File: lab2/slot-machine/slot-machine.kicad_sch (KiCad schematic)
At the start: 22 parts

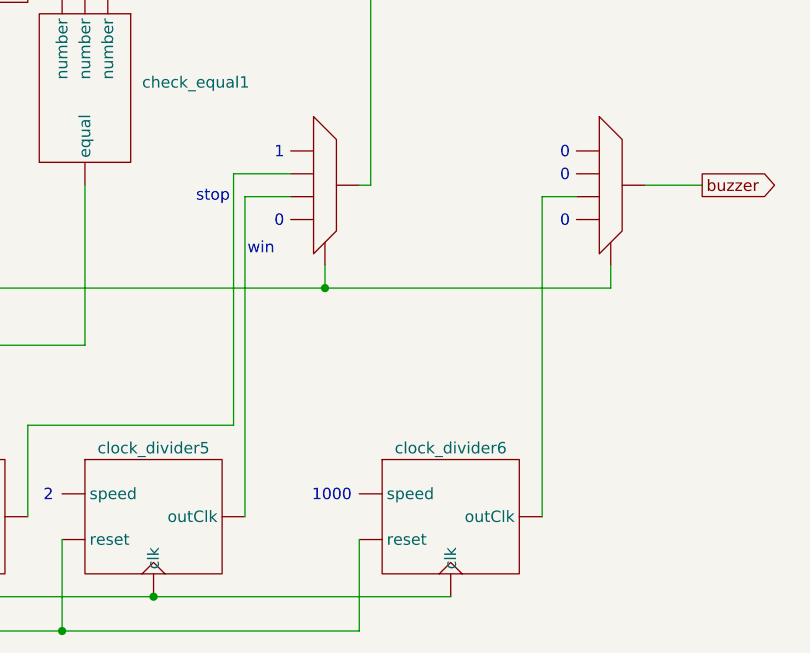
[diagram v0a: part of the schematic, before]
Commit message: update block diagram
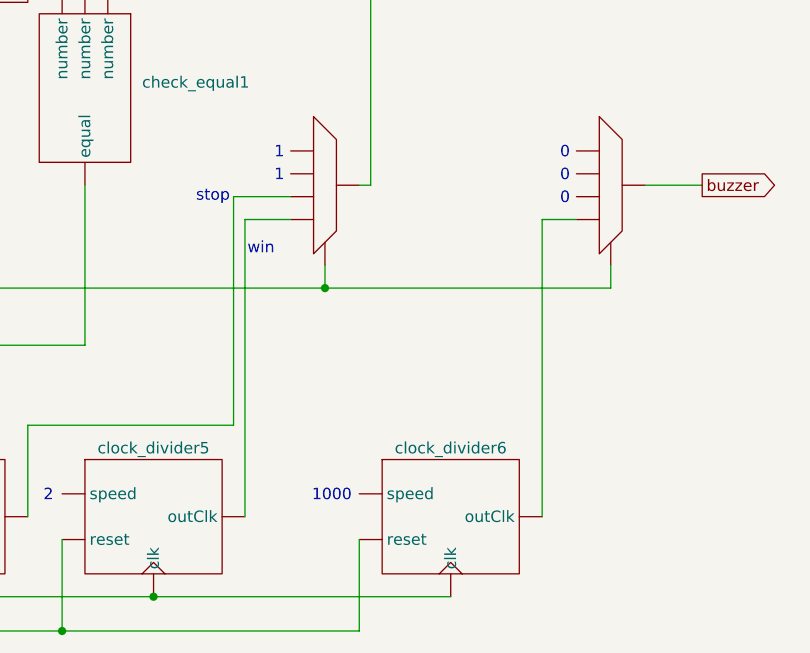
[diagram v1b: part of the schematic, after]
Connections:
- net at LFSR3. (reset): now also bin_to_bcd3. (bin), check_equal1. (number); no longer clock_divider3. (speed)
- net at U1.: now also FSM1. (start/stop), U2.
- net at bin_to_bcd2. (bin): now also 7_seg_encoder3. (en); no longer 7_seg_encoder4. (en)
- net at bin_to_bcd3. (bin): now also 7_seg_encoder5. (en); no longer 7_seg_encoder6. (en)
- net at bin_to_bcd1. (bin): now also 7_seg_encoder2. (en); no longer 7_seg_encoder1. (en)
- new net: FSM1. (start/stop), LFSR1. (reset), LFSR2. (reset), LFSR3. (reset), clock_divider1. (speed), clock_divider2. (speed), clock_divider3. (speed), clock_divider4. (speed), clock_divider5. (speed), clock_divider6. (speed)
- new net: FSM1. (start/stop), LFSR1. (reset), LFSR2. (reset), LFSR3. (reset)
- new net: LFSR1. (reset), bin_to_bcd1. (bin), check_equal1. (number)
- new net: LFSR3. (reset), clock_divider3. (speed)
- new net: LFSR2. (reset), bin_to_bcd2. (bin), check_equal1. (number)
- new net: 7_seg_encoder1. (en), 7_seg_encoder2. (en), 7_seg_encoder3. (en), 7_seg_encoder4. (en), 7_seg_encoder5. (en), 7_seg_encoder6. (en), U1.
- new net: U1., clock_divider5. (speed)
- new net: U1., clock_divider4. (speed)
- new net: 7_seg_encoder4. (en), bin_to_bcd2. (bin)
- new net: 7_seg_encoder6. (en), bin_to_bcd3. (bin)
- new net: 7_seg_encoder1. (en), bin_to_bcd1. (bin)
- new net: U2., clock_divider6. (speed)
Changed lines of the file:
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@@
 	(wire
 		(pts
-			(xy 133.35 140.97) (xy 133.35 105.41)
+			(xy 133.35 140.97) (xy 133.35 107.95)
 		)
 		(stroke
@@
 	(wire
 		(pts
-			(xy 133.35 105.41) (xy 137.16 105.41)
+			(xy 133.35 107.95) (xy 137.16 107.95)
 		)
 		(stroke
@@
 	(wire
 		(pts
-			(xy 100.33 105.41) (xy 105.41 105.41)
-		)
-		(stroke
-			(width 0)
-			(type default)
-		)
-	)
-	(wire
-		(pts
-			(xy 99.06 130.81) (xy 99.06 102.87)
+			(xy 100.33 107.95) (xy 105.41 107.95)
+		)
+		(stroke
+			(width 0)
+			(type default)
+		)
+	)
+	(wire
+		(pts
+			(xy 99.06 130.81) (xy 99.06 105.41)
 		)
 		(stroke
@@
 	(wire
 		(pts
-			(xy 100.33 140.97) (xy 100.33 105.41)
+			(xy 100.33 140.97) (xy 100.33 107.95)
 		)
 		(stroke
@@
 	(wire
 		(pts
-			(xy 99.06 102.87) (xy 105.41 102.87)
+			(xy 99.06 105.41) (xy 105.41 105.41)
 		)
 		(stroke
@@
 		)
 	)
+	(text "10"
+		(exclude_from_sim no)
+		(at 27.432 54.864 0)
+		(effects
+			(font
+				(size 1.27 1.27)
+			)
+		)
+	)
+	(text "stop"
+		(exclude_from_sim no)
+		(at 96.774 105.41 0)
+		(effects
+			(font
+				(size 1.27 1.27)
+			)
+		)
+	)
+	(text "7-bit"
+		(exclude_from_sim no)
+		(at 82.55 77.47 0)
+		(effects
+			(font
+				(size 1.27 1.27)
+			)
+		)
+	)
+	(text "7-bit"
+		(exclude_from_sim no)
+		(at 83.058 56.134 0)
+		(effects
+			(font
+				(size 1.27 1.27)
+			)
+		)
+	)
+	(text "1000"
+		(exclude_from_sim no)
+		(at 109.982 138.684 0)
+		(effects
+			(font
+				(size 1.27 1.27)
+			)
+		)
+	)
+	(text "5"
+		(exclude_from_sim no)
+		(at 28.194 33.274 0)
+		(effects
+			(font
+				(size 1.27 1.27)
+			)
+		)
+	)
 	(text "0"
 		(exclude_from_sim no)
-		(at 135.89 108.204 0)
-		(effects
-			(font
-				(size 1.27 1.27)
-			)
-		)
-	)
-	(text "10"
-		(exclude_from_sim no)
-		(at 27.432 54.864 0)
+		(at 135.89 100.584 0)
+		(effects
+			(font
+				(size 1.27 1.27)
+			)
+		)
+	)
+	(text "7-bit"
+		(exclude_from_sim no)
+		(at 83.058 34.544 0)
+		(effects
+			(font
+				(size 1.27 1.27)
+			)
+		)
+	)
+	(text "1"
+		(exclude_from_sim no)
+		(at 54.356 138.684 0)
+		(effects
+			(font
+				(size 1.27 1.27)
+			)
+		)
+	)
+	(text "2-bit"
+		(exclude_from_sim no)
+		(at 61.214 114.3 0)
+		(effects
+			(font
+				(size 1.27 1.27)
+			)
+		)
+	)
+	(text "20"
+		(exclude_from_sim no)
+		(at 27.432 76.454 0)
+		(effects
+			(font
+				(size 1.27 1.27)
+			)
+		)
+	)
+	(text "1"
+		(exclude_from_sim no)
+		(at 104.14 103.124 0)
 		(effects
 			(font
@@
 	(text "0"
 		(exclude_from_sim no)
-		(at 104.14 108.204 0)
-		(effects
-			(font
-				(size 1.27 1.27)
-			)
-		)
-	)
-	(text "stop"
-		(exclude_from_sim no)
-		(at 96.774 105.41 0)
-		(effects
-			(font
-				(size 1.27 1.27)
-			)
-		)
-	)
-	(text "7-bit"
-		(exclude_from_sim no)
-		(at 82.55 77.47 0)
-		(effects
-			(font
-				(size 1.27 1.27)
-			)
-		)
-	)
-	(text "7-bit"
-		(exclude_from_sim no)
-		(at 83.058 56.134 0)
-		(effects
-			(font
-				(size 1.27 1.27)
-			)
-		)
-	)
-	(text "1000"
-		(exclude_from_sim no)
-		(at 109.982 138.684 0)
-		(effects
-			(font
-				(size 1.27 1.27)
-			)
-		)
-	)
-	(text "5"
-		(exclude_from_sim no)
-		(at 28.194 33.274 0)
-		(effects
-			(font
-				(size 1.27 1.27)
-			)
-		)
-	)
-	(text "0"
-		(exclude_from_sim no)
-		(at 135.89 100.584 0)
-		(effects
-			(font
-				(size 1.27 1.27)
-			)
-		)
-	)
-	(text "7-bit"
-		(exclude_from_sim no)
-		(at 83.058 34.544 0)
-		(effects
-			(font
-				(size 1.27 1.27)
-			)
-		)
-	)
-	(text "1"
-		(exclude_from_sim no)
-		(at 54.356 138.684 0)
-		(effects
-			(font
-				(size 1.27 1.27)
-			)
-		)
-	)
-	(text "2-bit"
-		(exclude_from_sim no)
-		(at 61.214 114.3 0)
-		(effects
-			(font
-				(size 1.27 1.27)
-			)
-		)
-	)
-	(text "20"
-		(exclude_from_sim no)
-		(at 27.432 76.454 0)
+		(at 135.89 105.664 0)
 		(effects
 			(font
@@
 	)
 	(symbol
-		(lib_name "slot-machine:seven_seg_encoder")
 		(lib_id "slot-machine:seven_seg_encoder")
 		(at 125.73 60.96 0)
@@
 	)
 	(symbol
-		(lib_name "slot-machine:seven_seg_encoder")
 		(lib_id "slot-machine:seven_seg_encoder")
 		(at 125.73 78.74 0)
@@
 	)
 	(symbol
-		(lib_name "slot-machine:clock_divider")
 		(lib_id "slot-machine:clock_divider")
 		(at 90.17 140.97 0)
@@
 	)
 	(symbol
-		(lib_name "slot-machine:seven_seg_encoder")
 		(lib_id "slot-machine:seven_seg_encoder")
 		(at 125.73 34.29 0)
@@
 	)
 	(symbol
-		(lib_name "slot-machine:clock_divider")
 		(lib_id "slot-machine:clock_divider")
 		(at 66.04 140.97 0)
@@
 	)
 	(symbol
-		(lib_name "slot-machine:clock_divider")
 		(lib_id "slot-machine:clock_divider")
 		(at 123.19 140.97 0)
@@
 	)
 	(symbol
-		(lib_name "slot-machine:seven_seg_encoder")
 		(lib_id "slot-machine:seven_seg_encoder")
 		(at 125.73 69.85 0)
@@
 	)
 	(symbol
-		(lib_name "slot-machine:seven_seg_encoder")
 		(lib_id "slot-machine:seven_seg_encoder")
 		(at 125.73 43.18 0)
@@
 	)
 	(symbol
-		(lib_name "slot-machine:seven_seg_encoder")
 		(lib_id "slot-machine:seven_seg_encoder")
 		(at 125.73 52.07 0)
@@
 	)
 	(symbol
-		(lib_name "slot-machine:4_bit_mux")
 		(lib_id "slot-machine:4_bit_mux")
 		(at 140.97 104.14 0)
